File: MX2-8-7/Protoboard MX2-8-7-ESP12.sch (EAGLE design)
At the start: 145 parts, among them X1 ESP-12E

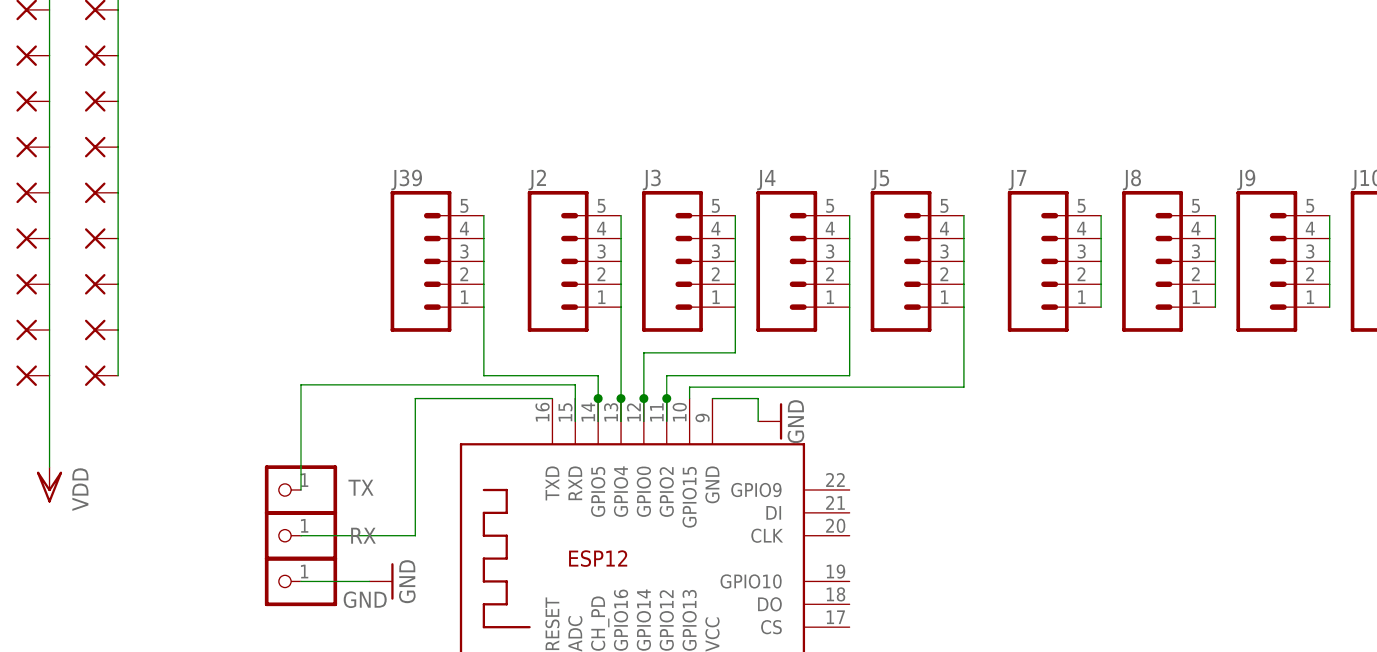
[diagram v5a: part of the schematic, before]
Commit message: Fixed revert and sccidental deletion
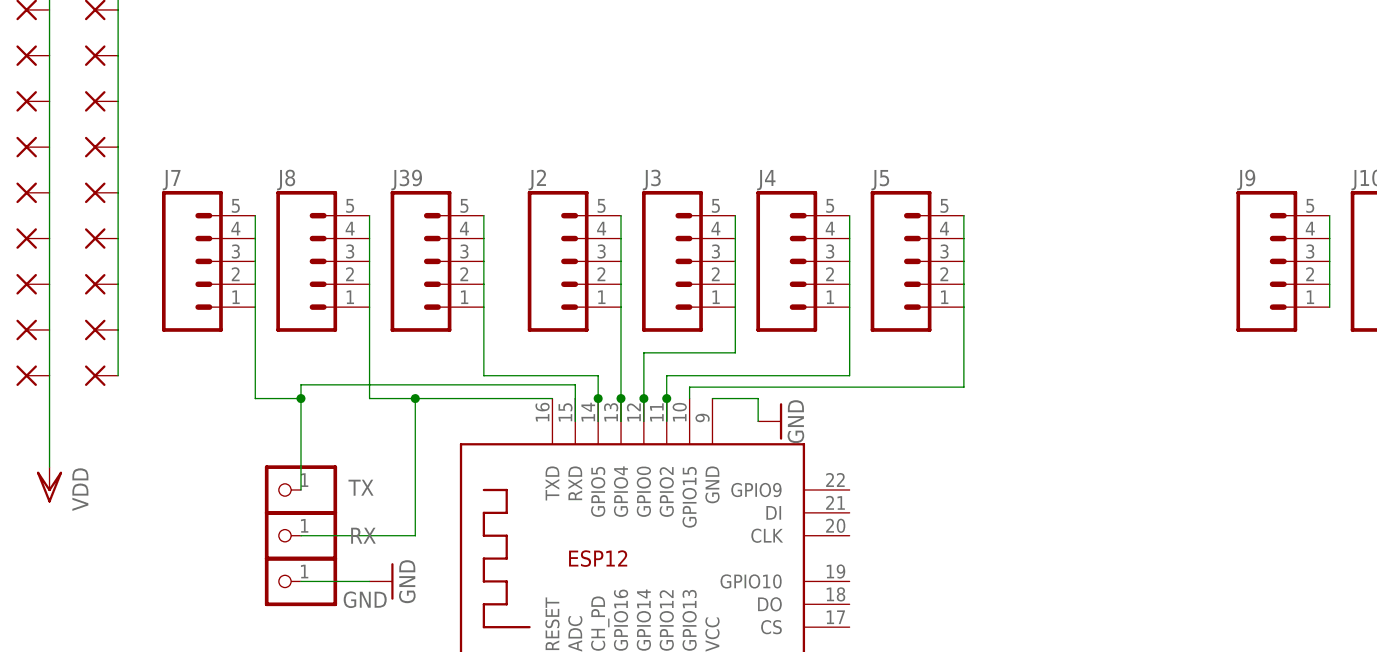
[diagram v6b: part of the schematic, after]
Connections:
- removed net N$7: J7.1, J7.2, J7.3, J7.4, J7.5
- removed net N$8: J8.1, J8.2, J8.3, J8.4, J8.5
- net N$45: now also J7.1, J7.2, J7.3, J7.4, J7.5
- net N$46: now also J8.1, J8.2, J8.3, J8.4, J8.5
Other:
- moved on the sheet: J7, J8
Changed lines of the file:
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@@
 <?xml version="1.0" encoding="utf-8"?>
 <!DOCTYPE eagle SYSTEM "eagle.dtd">
-<eagle version="7.7.0">
+<eagle version="7.6.0">
 <drawing>
 <settings>
@@
 <instance part="J26" gate="G$1" x="132.08" y="-35.56"/>
 <instance part="J27" gate="G$1" x="144.78" y="-35.56"/>
-<instance part="J7" gate="G$1" x="137.16" y="40.64"/>
-<instance part="J8" gate="G$1" x="149.86" y="40.64"/>
+<instance part="J7" gate="G$1" x="43.18" y="40.64"/>
+<instance part="J8" gate="G$1" x="55.88" y="40.64"/>
 <instance part="J9" gate="G$1" x="162.56" y="40.64"/>
 <instance part="J10" gate="G$1" x="175.26" y="40.64"/>
@@
 </segment>
 </net>
-<net name="N$7" class="0">
-<segment>
-<pinref part="J7" gate="G$1" pin="5"/>
-<pinref part="J7" gate="G$1" pin="4"/>
-<wire x1="144.78" y1="45.72" x2="144.78" y2="43.18" width="0.1524" layer="91"/>
-<pinref part="J7" gate="G$1" pin="3"/>
-<wire x1="144.78" y1="43.18" x2="144.78" y2="40.64" width="0.1524" layer="91"/>
-<pinref part="J7" gate="G$1" pin="2"/>
-<wire x1="144.78" y1="40.64" x2="144.78" y2="38.1" width="0.1524" layer="91"/>
-<pinref part="J7" gate="G$1" pin="1"/>
-<wire x1="144.78" y1="38.1" x2="144.78" y2="35.56" width="0.1524" layer="91"/>
-</segment>
-</net>
-<net name="N$8" class="0">
-<segment>
-<pinref part="J8" gate="G$1" pin="1"/>
-<pinref part="J8" gate="G$1" pin="2"/>
-<wire x1="157.48" y1="35.56" x2="157.48" y2="38.1" width="0.1524" layer="91"/>
-<pinref part="J8" gate="G$1" pin="3"/>
-<wire x1="157.48" y1="38.1" x2="157.48" y2="40.64" width="0.1524" layer="91"/>
-<pinref part="J8" gate="G$1" pin="4"/>
-<wire x1="157.48" y1="40.64" x2="157.48" y2="43.18" width="0.1524" layer="91"/>
-<pinref part="J8" gate="G$1" pin="5"/>
-<wire x1="157.48" y1="43.18" x2="157.48" y2="45.72" width="0.1524" layer="91"/>
-</segment>
-</net>
 <net name="N$9" class="0">
 <segment>
@@
 <wire x1="68.58" y1="10.16" x2="55.88" y2="10.16" width="0.1524" layer="91"/>
 <pinref part="X1" gate="G$1" pin="TXD"/>
+<pinref part="J8" gate="G$1" pin="1"/>
+<pinref part="J8" gate="G$1" pin="2"/>
+<wire x1="63.5" y1="35.56" x2="63.5" y2="38.1" width="0.1524" layer="91"/>
+<pinref part="J8" gate="G$1" pin="3"/>
+<wire x1="63.5" y1="38.1" x2="63.5" y2="40.64" width="0.1524" layer="91"/>
+<pinref part="J8" gate="G$1" pin="4"/>
+<wire x1="63.5" y1="40.64" x2="63.5" y2="43.18" width="0.1524" layer="91"/>
+<pinref part="J8" gate="G$1" pin="5"/>
+<wire x1="63.5" y1="43.18" x2="63.5" y2="45.72" width="0.1524" layer="91"/>
+<wire x1="68.58" y1="25.4" x2="63.5" y2="25.4" width="0.1524" layer="91"/>
+<wire x1="63.5" y1="25.4" x2="63.5" y2="35.56" width="0.1524" layer="91"/>
+<junction x="68.58" y="25.4"/>
 </segment>
 </net>
@@
 <wire x1="86.36" y1="25.4" x2="86.36" y2="26.924" width="0.1524" layer="91"/>
 <pinref part="TX" gate="G$1" pin="1"/>
-<wire x1="55.88" y1="26.924" x2="55.88" y2="15.24" width="0.1524" layer="91"/>
+<wire x1="55.88" y1="26.924" x2="55.88" y2="25.4" width="0.1524" layer="91"/>
+<wire x1="55.88" y1="25.4" x2="55.88" y2="15.24" width="0.1524" layer="91"/>
 <wire x1="86.36" y1="26.924" x2="55.88" y2="26.924" width="0.1524" layer="91"/>
-</segment>
-</net>
+<pinref part="J7" gate="G$1" pin="5"/>
+<pinref part="J7" gate="G$1" pin="4"/>
+<wire x1="50.8" y1="45.72" x2="50.8" y2="43.18" width="0.1524" layer="91"/>
+<pinref part="J7" gate="G$1" pin="3"/>
+<wire x1="50.8" y1="43.18" x2="50.8" y2="40.64" width="0.1524" layer="91"/>
+<pinref part="J7" gate="G$1" pin="2"/>
+<wire x1="50.8" y1="40.64" x2="50.8" y2="38.1" width="0.1524" layer="91"/>
+<pinref part="J7" gate="G$1" pin="1"/>
+<wire x1="50.8" y1="38.1" x2="50.8" y2="35.56" width="0.1524" layer="91"/>
+<wire x1="55.88" y1="25.4" x2="50.8" y2="25.4" width="0.1524" layer="91"/>
+<wire x1="50.8" y1="25.4" x2="50.8" y2="35.56" width="0.1524" layer="91"/>
+<junction x="55.88" y="25.4"/>
+</segment>
+</net>

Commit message: Silkscreen text fixes
Silkscreen text fixes
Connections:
- net N$45: now also RX.1; no longer TX.1
- net N$46: now also TX.1; no longer RX.1
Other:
- moved on the sheet: RX, TX
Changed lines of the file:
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@@
 <?xml version="1.0" encoding="utf-8"?>
 <!DOCTYPE eagle SYSTEM "eagle.dtd">
-<eagle version="7.6.0">
+<eagle version="7.7.0">
 <drawing>
 <settings>
@@
 <part name="J29" library="SparkFun-Connectors" deviceset="M05" device="NO_SILK"/>
 <part name="J30" library="SparkFun-Connectors" deviceset="M05" device="NO_SILK"/>
+<part name="RX" library="adafruit" deviceset="PINHD-1X1" device="CB"/>
 <part name="TX" library="adafruit" deviceset="PINHD-1X1" device="CB"/>
-<part name="RX" library="adafruit" deviceset="PINHD-1X1" device="CB"/>
 <part name="GND" library="adafruit" deviceset="PINHD-1X1" device="CB"/>
 <part name="GND6" library="supply1" deviceset="GND" device=""/>
@@
 <instance part="J29" gate="G$1" x="172.72" y="-35.56"/>
 <instance part="J30" gate="G$1" x="330.2" y="-30.48"/>
-<instance part="TX" gate="G$1" x="53.34" y="15.24" smashed="yes" rot="R180">
+<instance part="RX" gate="G$1" x="53.34" y="15.24" smashed="yes" rot="R180">
 <attribute name="NAME" x="64.008" y="16.383" size="1.778" layer="95" rot="R180"/>
 <attribute name="VALUE" x="59.69" y="20.32" size="1.778" layer="96" rot="R180"/>
 </instance>
-<instance part="RX" gate="G$1" x="53.34" y="10.16" smashed="yes" rot="R180">
+<instance part="TX" gate="G$1" x="53.34" y="10.16" smashed="yes" rot="R180">
 <attribute name="NAME" x="64.262" y="11.049" size="1.778" layer="95" rot="R180"/>
 <attribute name="VALUE" x="59.69" y="15.24" size="1.778" layer="96" rot="R180"/>
@@
 <wire x1="83.82" y1="25.4" x2="68.58" y2="25.4" width="0.1524" layer="91"/>
 <wire x1="68.58" y1="25.4" x2="68.58" y2="10.16" width="0.1524" layer="91"/>
-<pinref part="RX" gate="G$1" pin="1"/>
+<pinref part="TX" gate="G$1" pin="1"/>
 <wire x1="68.58" y1="10.16" x2="55.88" y2="10.16" width="0.1524" layer="91"/>
 <pinref part="X1" gate="G$1" pin="TXD"/>
@@
 <wire x1="86.36" y1="22.86" x2="86.36" y2="25.4" width="0.1524" layer="91"/>
 <wire x1="86.36" y1="25.4" x2="86.36" y2="26.924" width="0.1524" layer="91"/>
-<pinref part="TX" gate="G$1" pin="1"/>
+<pinref part="RX" gate="G$1" pin="1"/>
 <wire x1="55.88" y1="26.924" x2="55.88" y2="25.4" width="0.1524" layer="91"/>
 <wire x1="55.88" y1="25.4" x2="55.88" y2="15.24" width="0.1524" layer="91"/>
